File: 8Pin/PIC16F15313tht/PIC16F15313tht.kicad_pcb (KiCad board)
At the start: 2 copper layers, 18 parts, among them J1 JACK DC, J2 USB_B, J3 TERMINAL BLOCK, J4 Conn_02x02_Odd_Even, J5 ICSP, J6 terminales, J7 terminales, SW1 RESET, SW2 CONTROL, U1 PIC16F15313

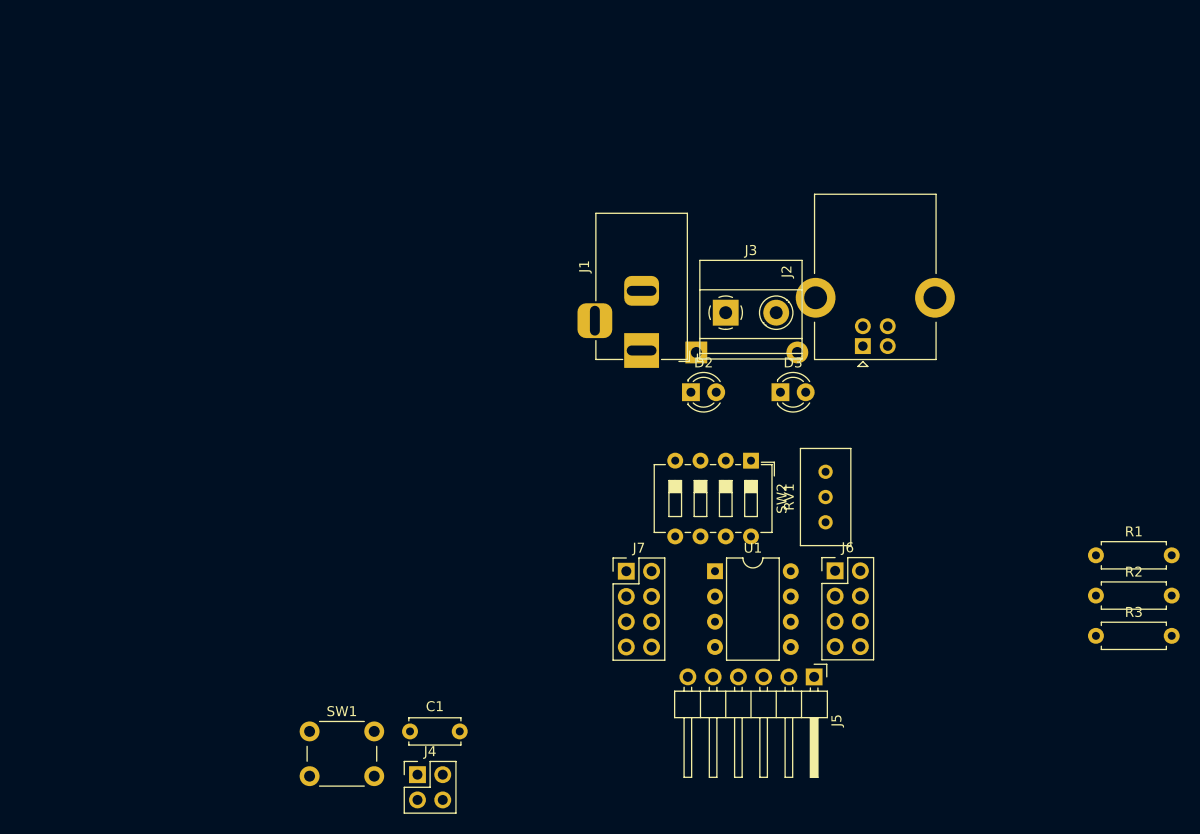
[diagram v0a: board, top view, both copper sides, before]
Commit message: Se terminó la huella del tp4056
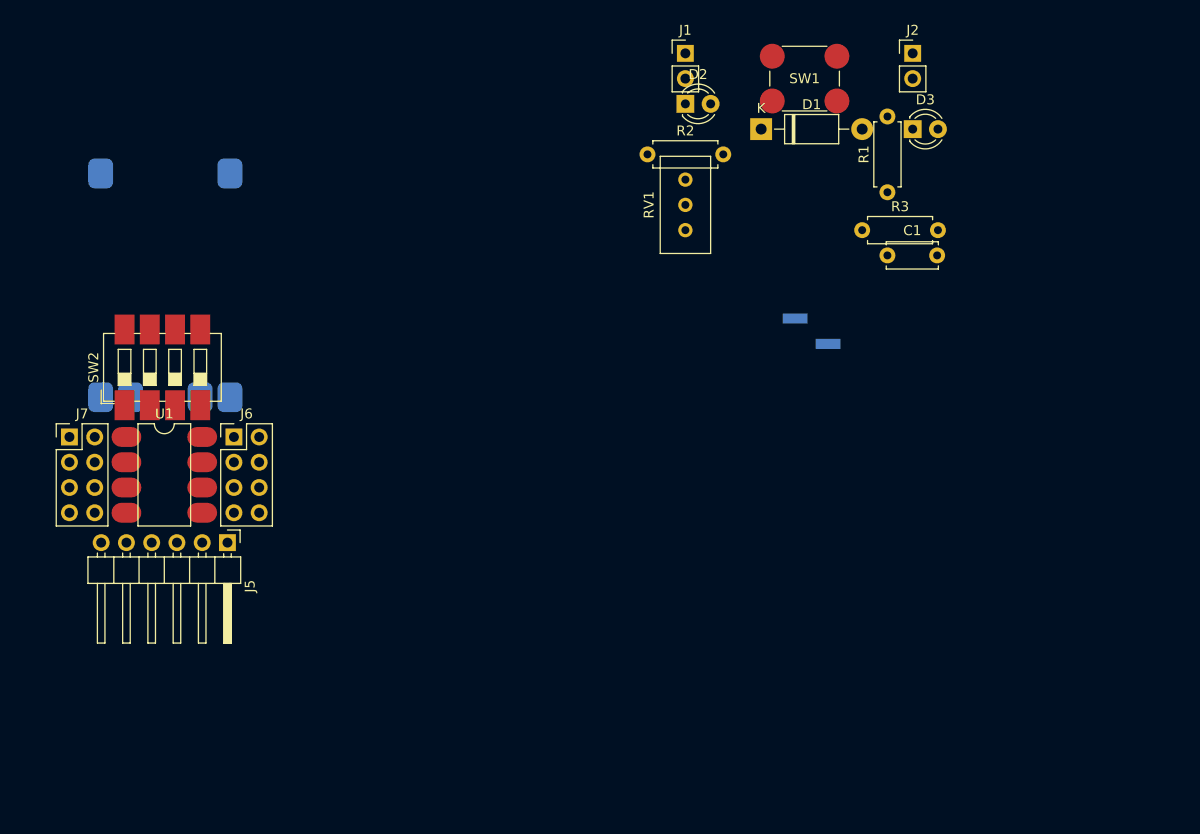
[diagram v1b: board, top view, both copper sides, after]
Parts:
- removed J3: TERMINAL BLOCK, TerminalBlock_Phoenix:TerminalBlock_Phoenix_MKDS-1,5-2-5.08_1x02_P5.08mm_Horizontal
- removed J4: Conn_02x02_Odd_Even, Connector_PinHeader_2.54mm:PinHeader_2x02_P2.54mm_Vertical
- added BT1: LI-PO, Connector_PinHeader_2.54mm:PinHeader_1x02_P2.54mm_Vertical_SMD_Pin1Right, B.Cu at (165.1, 86.4)
- added Mod1: TP4056, CreatedFootprints:TP4056, B.Cu at (87.6, 81.5)
- D1: moved to F.Cu
- J1: value JACK DC -> Conn_01x02; footprint Connector_BarrelJack:BarrelJack_Horizontal -> Connector_PinHeader_2.54mm:PinHeader_1x02_P2.54mm_Vertical
- J2: value USB_B -> Conn_01x02; footprint Connector_USB:USB_B_Lumberg_2411_02_Horizontal -> Connector_PinHeader_2.54mm:PinHeader_1x02_P2.54mm_Vertical
- moved SW1 82.3 mm to (161.1, 58.7)
- moved C1 67.8 mm to (172.7, 78.7)
- moved R2 63.3 mm to (148.6, 68.6)
- moved SW2 63.2 mm to (96.0, 93.8), turned to 90 degrees
- moved J6 61.9 mm to (107.0, 97.0)
- moved U1 60.7 mm to (96.2, 97.0)
- moved J5 60.5 mm to (106.3, 107.6)
- moved J7 57.6 mm to (90.5, 97.0)
- moved R3 47.1 mm to (170.2, 76.2)
- moved R1 42.1 mm to (172.7, 72.4), turned to 90 degrees
- moved RV1 32.6 mm to (152.4, 71.1)
- moved J1 30.2 mm to (152.4, 58.4), turned to 0 degrees
- moved J2 29.9 mm to (175.3, 58.4), turned to 0 degrees
- moved D3 29.6 mm to (175.3, 66.0)
- moved D2 29.0 mm to (152.4, 63.5)
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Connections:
- J1 pad 1: VCC -> Net-(D1-A)
- J1 pad 2: /on/off -> Net-(D1-A)
- J2 pad 1: VCC -> GND
- J2 pad 2: unconnected-(J2-D--Pad2) -> GND
- SW2 pad 1: /on/off -> /bat_vcc
- SW2 pad 8: GND -> VCC

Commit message: finalizacion de la tarjeta
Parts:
- removed BT1: LI-PO, Connector_PinHeader_2.54mm:PinHeader_1x02_P2.54mm_Vertical_SMD_Pin1Right
- added J3: Conn_01x01, TestPoint:TestPoint_Pad_D2.5mm, B.Cu at (92.5, 101.0)
- added J4: Conn_01x01, TestPoint:TestPoint_Pad_D2.5mm, B.Cu at (107.5, 101.0)
- moved D3 86.0 mm to (90.5, 80.5), turned to 90 degrees
- moved C1 80.8 mm to (92.2, 86.5), turned to 180 degrees
- moved R3 76.2 mm to (94.3, 83.5), turned to 180 degrees
- moved R1 67.9 mm to (105.7, 83.5), turned to 0 degrees
- moved J2 66.9 mm to (110.5, 75.0), turned to 180 degrees
- moved D1 66.6 mm to (94.8, 79.5)
- moved SW1 65.8 mm to (96.8, 72.2)
- moved J1 65.1 mm to (89.5, 75.0), turned to 180 degrees
- moved R2 54.3 mm to (96.2, 82.8)
- moved D2 46.2 mm to (109.5, 80.5), turned to 90 degrees
- moved RV1 44.5 mm to (111.0, 87.4)
- moved J6 3.00 mm to (110.0, 97.0)
- moved J7 3.00 mm to (87.5, 97.0)
- moved Mod1 2.00 mm to (87.5, 83.5)
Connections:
- J1 pad 2: Net-(D1-A) -> GND
- J2 pad 1: GND -> Net-(D1-A)
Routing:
- net VCC: track 0.00 -> 41.6 mm, vias 0 -> 4
- net /ra3: track 0.00 -> 36.8 mm, vias 0 -> 2
- net /pgd: track 0.00 -> 32.6 mm
- net GND: track 0.00 -> 29.9 mm
- net /reset: track 0.00 -> 28.0 mm
- net Net-(D1-A): track 0.00 -> 27.8 mm
- net /ra5: track 0.00 -> 25.3 mm
- net /led_op: track 0.00 -> 19.0 mm, vias 0 -> 1
- net /pgc: track 0.00 -> 16.6 mm
- net /pot: track 0.00 -> 8.97 mm
- net /ra4: track 0.00 -> 8.73 mm
- net /ra2: track 0.00 -> 8.73 mm
- net /bat_vcc: track 0.00 -> 8.72 mm, vias 0 -> 1
- net Net-(J4-Pin_1): track 0.00 -> 7.66 mm
- net Net-(J3-Pin_1): track 0.00 -> 7.66 mm
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- added copper zone on B.Cu, net GND
- added copper zone on F.Cu, net VCC
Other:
- board outline added: 29 x 41.5 mm
- board text added: "+"
- board text added: "-"
- board text added: "1 batería 2 reset btn 3 led op 4 trimpot"
- board text added: "Diseño: Ing: Mucio Gómez Vieyra"
- board text added: "GND RA0 RA1 RA2"
- board text added: "GND VCC"
- board text added: "ICSP"
- board text added: "ON"
- board text added: "PIC16F15313"
- board text added: "RA0 trimpot RA3 reset RA5 led op"
- board text added: "VCC RA5 RA4 RA3"
- board text added: "mgv3d.com"
- board text added: "pecten μ"
- board text added: "pecten μ V0.1"

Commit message: se terminó la tarjeta y se exortaron archivos gerber
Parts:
- added G1: LOGO, LOGO, B.Cu at (100.5, 102.0)
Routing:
- net /ra3: track 36.8 -> 37.8 mm
